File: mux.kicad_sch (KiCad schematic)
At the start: 6 parts, among them U24002 4066, U24003 4066, U24004 4075

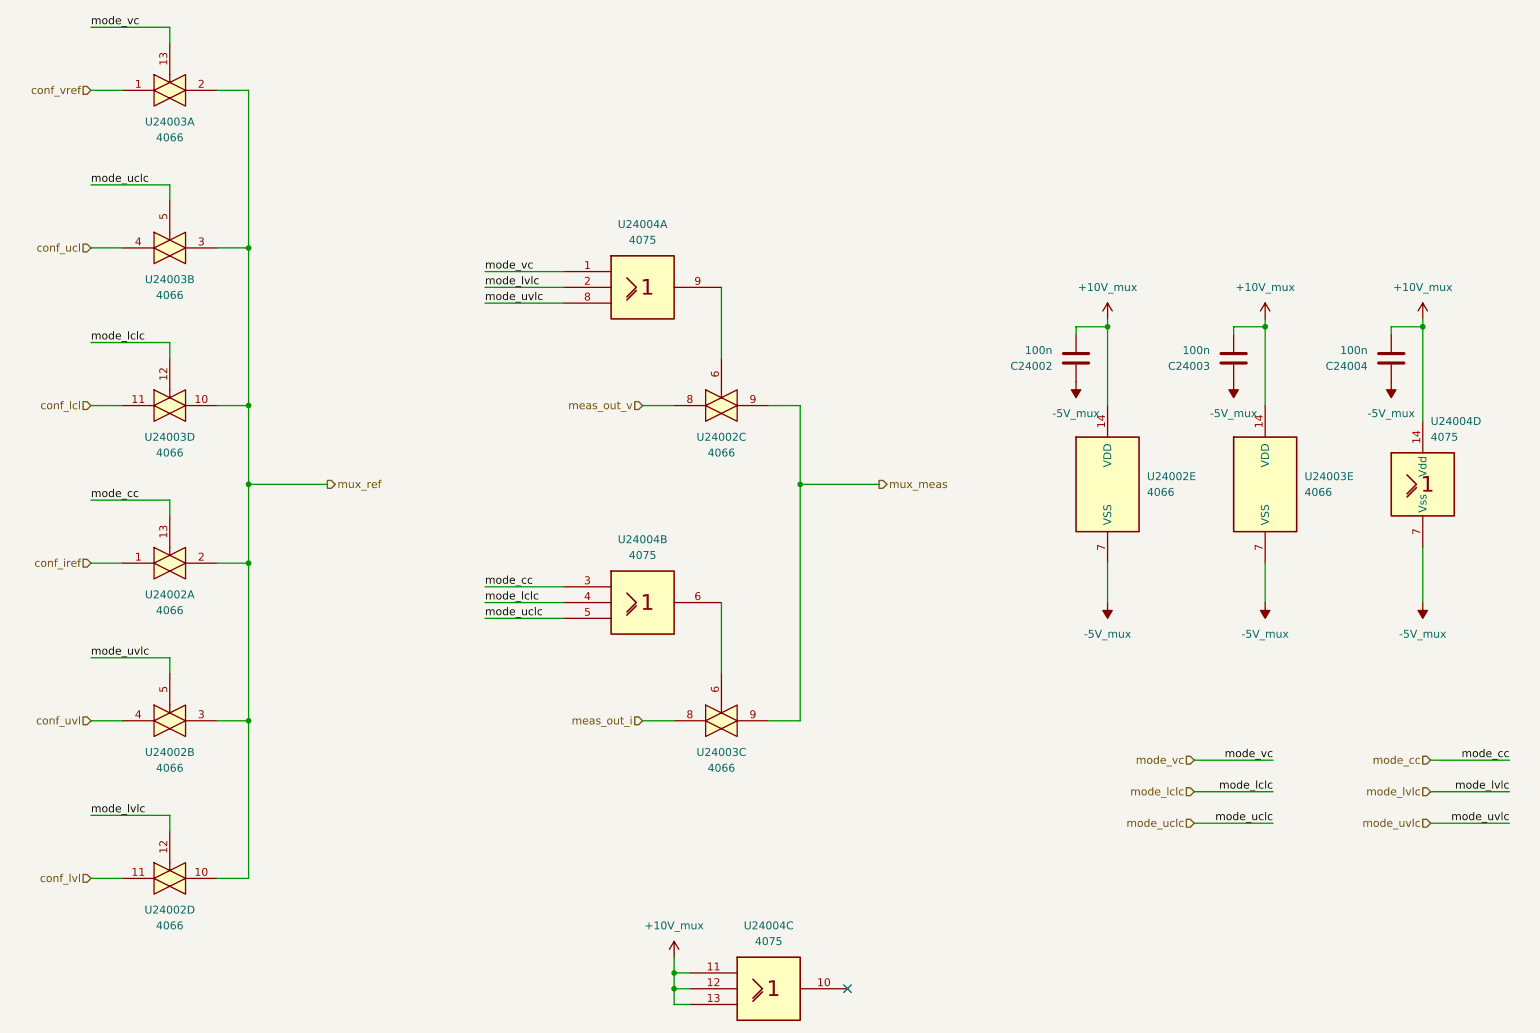
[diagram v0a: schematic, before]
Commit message: add pss 3dmodels and testpoints
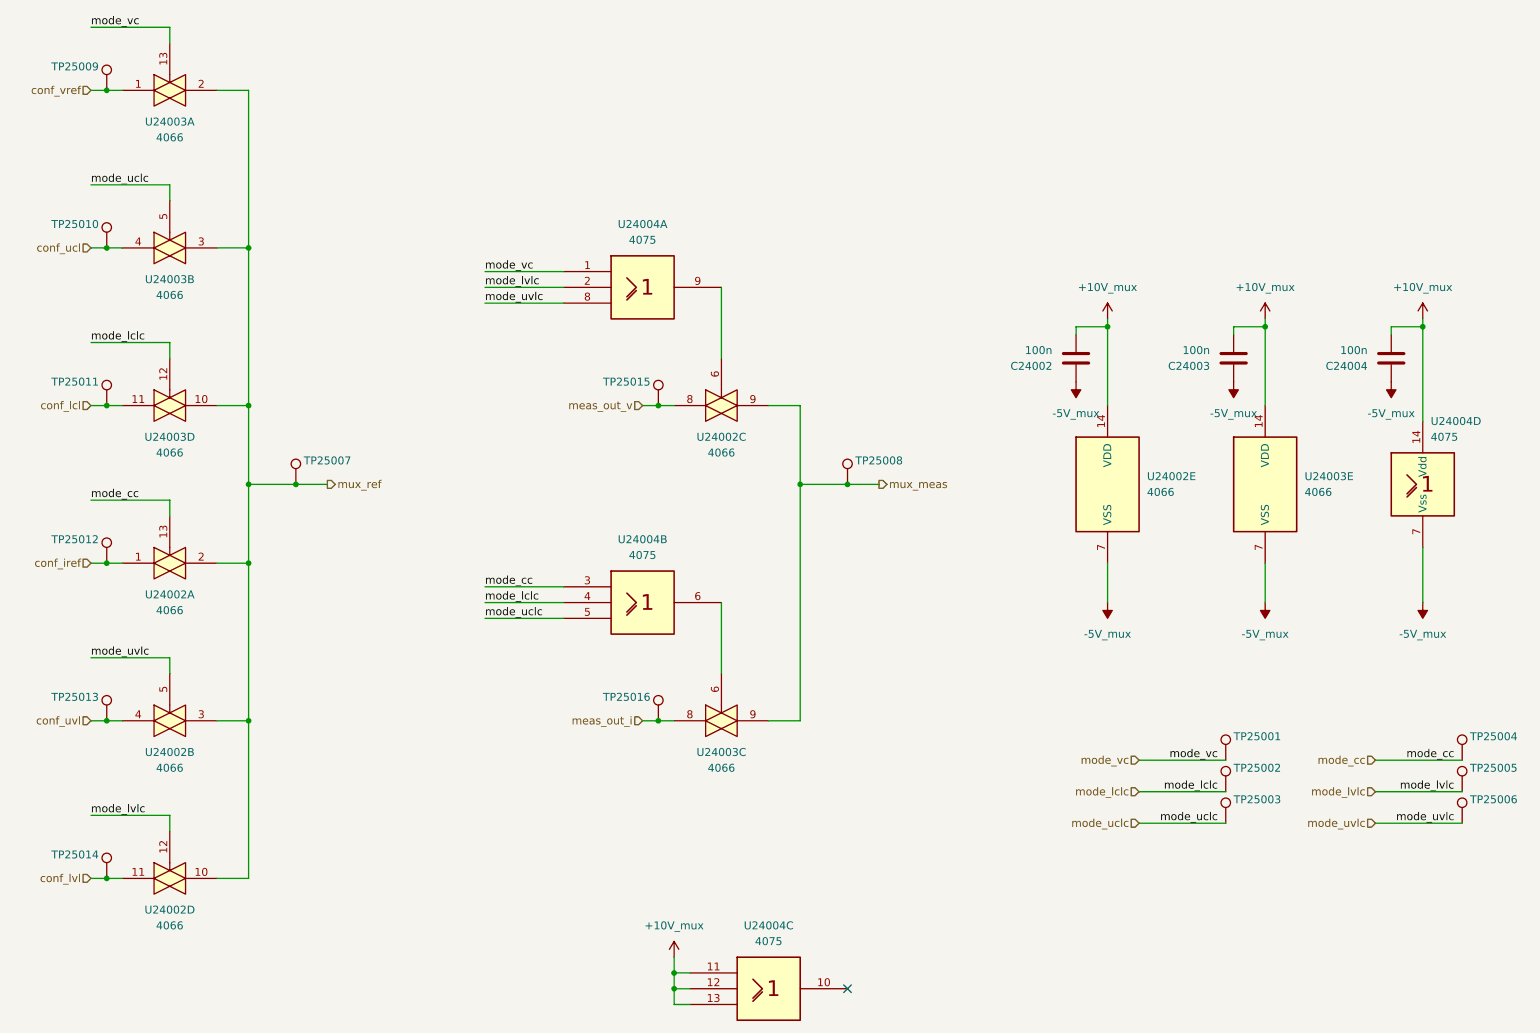
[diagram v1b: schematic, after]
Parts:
- added TP25001, TP25002, TP25003, TP25004, TP25005, TP25006, TP25007, TP25008, TP25009, TP25010, TP25011, TP25012, TP25013, TP25014, TP25015, TP25016: ~, pss:TP_0805_2012Metric, symbol Connector:TestPoint
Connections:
- net conf_iref: now also TP25012.1
- net conf_lcl: now also TP25011.1
- net conf_lvl: now also TP25014.1
- net conf_ucl: now also TP25010.1
- net conf_uvl: now also TP25013.1
- net conf_vref: now also TP25009.1
- net meas_out_i: now also TP25016.1
- net meas_out_v: now also TP25015.1
- net mode_cc: now also TP25004.1
- net mode_lclc: now also TP25002.1
- net mode_lvlc: now also TP25005.1
- net mode_uclc: now also TP25003.1
- net mode_uvlc: now also TP25006.1
- net mode_vc: now also TP25001.1
- net mux_meas: now also TP25008.1
- net mux_ref: now also TP25007.1

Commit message: edit pss symbol library: export all schematic symbols to library 'pss' and update symbol link
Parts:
- TP25001, TP25002, TP25003, TP25004, TP25005, TP25006, TP25007, TP25008, TP25009, TP25010, TP25011, TP25012, TP25013, TP25014, TP25015, TP25016: symbol Connector:TestPoint -> pss:TestPoint
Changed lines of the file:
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@@
 	)
 	(symbol
-		(lib_id "Connector:TestPoint")
+		(lib_id "pss:TestPoint")
 		(at 271.78 162.56 0)
 		(unit 1)
@@
 	)
 	(symbol
-		(lib_id "Connector:TestPoint")
+		(lib_id "pss:TestPoint")
 		(at 142.24 95.25 0)
 		(mirror y)
@@
 	)
 	(symbol
-		(lib_id "Connector:TestPoint")
+		(lib_id "pss:TestPoint")
 		(at 142.24 146.05 0)
 		(mirror y)
@@
 	)
 	(symbol
-		(lib_id "Connector:TestPoint")
+		(lib_id "pss:TestPoint")
 		(at 53.34 95.25 0)
 		(mirror y)
@@
 	)
 	(symbol
-		(lib_id "Connector:TestPoint")
+		(lib_id "pss:TestPoint")
 		(at 53.34 44.45 0)
 		(mirror y)
@@
 	)
 	(symbol
-		(lib_id "Connector:TestPoint")
+		(lib_id "pss:TestPoint")
 		(at 233.68 157.48 0)
 		(unit 1)
@@
 	)
 	(symbol
-		(lib_id "Connector:TestPoint")
+		(lib_id "pss:TestPoint")
 		(at 233.68 162.56 0)
 		(unit 1)
@@
 	)
 	(symbol
-		(lib_id "Connector:TestPoint")
+		(lib_id "pss:TestPoint")
 		(at 53.34 69.85 0)
 		(mirror y)
@@
 	)
 	(symbol
-		(lib_id "Connector:TestPoint")
+		(lib_id "pss:TestPoint")
 		(at 271.78 157.48 0)
 		(unit 1)
@@
 	)
 	(symbol
-		(lib_id "Connector:TestPoint")
+		(lib_id "pss:TestPoint")
 		(at 53.34 146.05 0)
 		(mirror y)
@@
 	)
 	(symbol
-		(lib_id "Connector:TestPoint")
+		(lib_id "pss:TestPoint")
 		(at 233.68 152.4 0)
 		(unit 1)
@@
 	)
 	(symbol
-		(lib_id "Connector:TestPoint")
+		(lib_id "pss:TestPoint")
 		(at 172.72 107.95 0)
 		(unit 1)
@@
 	)
 	(symbol
-		(lib_id "Connector:TestPoint")
+		(lib_id "pss:TestPoint")
 		(at 53.34 120.65 0)
 		(mirror y)
@@
 	)
 	(symbol
-		(lib_id "Connector:TestPoint")
+		(lib_id "pss:TestPoint")
 		(at 83.82 107.95 0)
 		(unit 1)
@@
 	)
 	(symbol
-		(lib_id "Connector:TestPoint")
+		(lib_id "pss:TestPoint")
 		(at 53.34 171.45 0)
 		(mirror y)
@@
 	)
 	(symbol
-		(lib_id "Connector:TestPoint")
+		(lib_id "pss:TestPoint")
 		(at 271.78 152.4 0)
 		(unit 1)
